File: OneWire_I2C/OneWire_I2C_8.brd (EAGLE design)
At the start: 22.2 x 28.2 mm, 14 parts, among them Q1 TP0602N3

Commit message: Added Schematic and board for DS2482-800
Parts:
- removed C1: (no value), SparkFun-Capacitors:0603-CAP
- removed Q1: TP0602N3, transistor-fet:TO-92
- removed R3: (no value), SparkFun-Resistors:AXIAL-0.4
- removed W1: DS2482-100, PuffinOneWIre:SOIC8
- added J2, J4, J5, J6, J7, J8: (no value), SparkFun-Connectors:1X03
- added J9: (no value), SparkFun-Connectors:1X06
- added SJ5: (no value), jumper:SJ
- added U$3: (no value), SparkFun-Electromechanical:STAND-OFF
- J1: device SparkFun-Connectors:1X05 -> SparkFun-Connectors:1X03
- J3: device SparkFun-Connectors:SCREWTERMINAL-3.5MM-3 -> SparkFun-Connectors:1X03
- R1, R2: device SparkFun-Resistors:0603-RES -> SparkFun-Passives:0603-RES
- SJ3: device jumper:SJ -> jumper:SJ_2
- U$1: value (none) -> DS2482-800; device SparkFun-Electromechanical:STAND-OFF-TIGHT -> Puffin:SOIC16
- U$2: device SparkFun-Electromechanical:STAND-OFF-TIGHT -> SparkFun-Electromechanical:STAND-OFF
- moved U$2 30.4 mm to (1.91, 2.54)
- moved J1 25.5 mm to (3.81, 22.9), turned to 90 degrees
- moved U$1 14.2 mm to (16.5, 16.5), turned to 90 degrees
- moved SJ3 13.4 mm to (5.08, 14.0)
- moved J3 8.64 mm to (8.89, 22.9), turned to 90 degrees
- moved SJ1 5.46 mm to (5.08, 6.35), turned to 0 degrees
- moved SJ2 5.46 mm to (5.08, 10.2), turned to 0 degrees
- moved R1 3.70 mm to (18.4, 6.35), turned to 0 degrees
- moved SJ4 3.70 mm to (14.6, 6.35), turned to 180 degrees
- moved R2 3.70 mm to (18.4, 10.2), turned to 0 degrees
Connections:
- removed net 1WR: J1.4, J3.2, Q1.3, W1.2
- removed net N$10: Q1.1, R3.P$1
- removed net N$3: R2.2, SJ3.2
- removed net N$4: R1.2, SJ4.2
- removed net PCTL: Q1.2, W1.6
- new net AD2: SJ3.2, U$1.6
- new net IO0: J1.2, J9.3, U$1.14
- new net IO1: J2.2, J9.2, U$1.15
- new net IO2: J3.2, U$1.16
- new net IO3: J4.2, U$1.1
- new net IO4: J5.2, U$1.12
- new net IO5: J6.2, U$1.11
- new net IO6: J7.2, U$1.10
- new net IO7: J8.2, U$1.9
- new net N$1: R1.1, SJ4.1
- new net N$2: R2.1, SJ5.1
- net AD0: now also U$1.8; no longer W1.8
- net AD1: now also U$1.7; no longer W1.7
- net GND: now also J1.3, J2.3, J4.3, J5.3, J6.3, J7.3, J8.3, J9.1, SJ3.3, U$1.13; no longer C1.2, J1.5, W1.3
- net SCL: now also J9.4, SJ4.2, U$1.2; no longer J1.2, SJ3.1, W1.4
- net SDA: now also J9.5, SJ5.2, U$1.3; no longer J1.3, SJ4.1, W1.5
- net VCC: now also J2.1, J4.1, J5.1, J6.1, J7.1, J8.1, J9.6, R1.2, R2.2, SJ3.1, U$1.4; no longer C1.1, R1.1, R2.1, R3.P$2, W1.1
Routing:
- net 1WR: track 42.4 -> 0.00 mm
- net IO0: track 0.00 -> 32.2 mm, vias 0 -> 2
- net IO1: track 0.00 -> 31.5 mm, vias 0 -> 2
- net AD2: track 0.00 -> 17.2 mm, vias 0 -> 2
- net AD0: track 9.08 -> 23.3 mm, vias 0 -> 2
- net IO3: track 0.00 -> 12.1 mm
- net SCL: track 23.7 -> 13.5 mm, vias 2 -> 0
- net IO7: track 0.00 -> 8.11 mm
- net IO4: track 0.00 -> 8.11 mm
- net N$10: track 7.93 -> 0.00 mm
- net IO2: track 0.00 -> 7.74 mm
- net IO6: track 0.00 -> 7.22 mm
- net IO5: track 0.00 -> 7.22 mm
- net PCTL: track 6.69 -> 0.00 mm
- net VCC: track 63.5 -> 69.3 mm
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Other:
- board size 22.2 x 28.2 mm -> 26.7 x 30.8 mm
- board text removed: "1WR"
- board text removed: "GND"
- board text removed: "SCL"
- board text removed: "SDA"
- board text removed: "VCC"

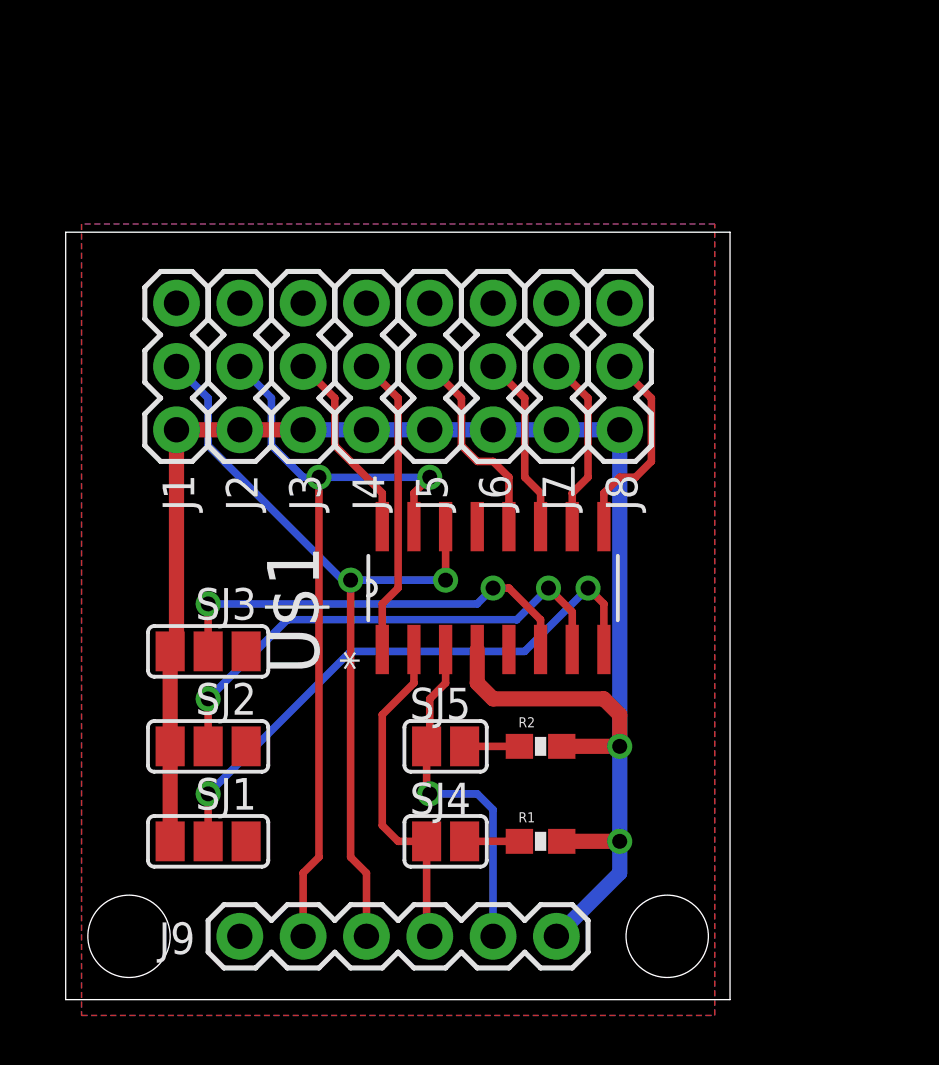
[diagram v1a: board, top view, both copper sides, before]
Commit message: Tweaks to I2C 1Wire bridge boards
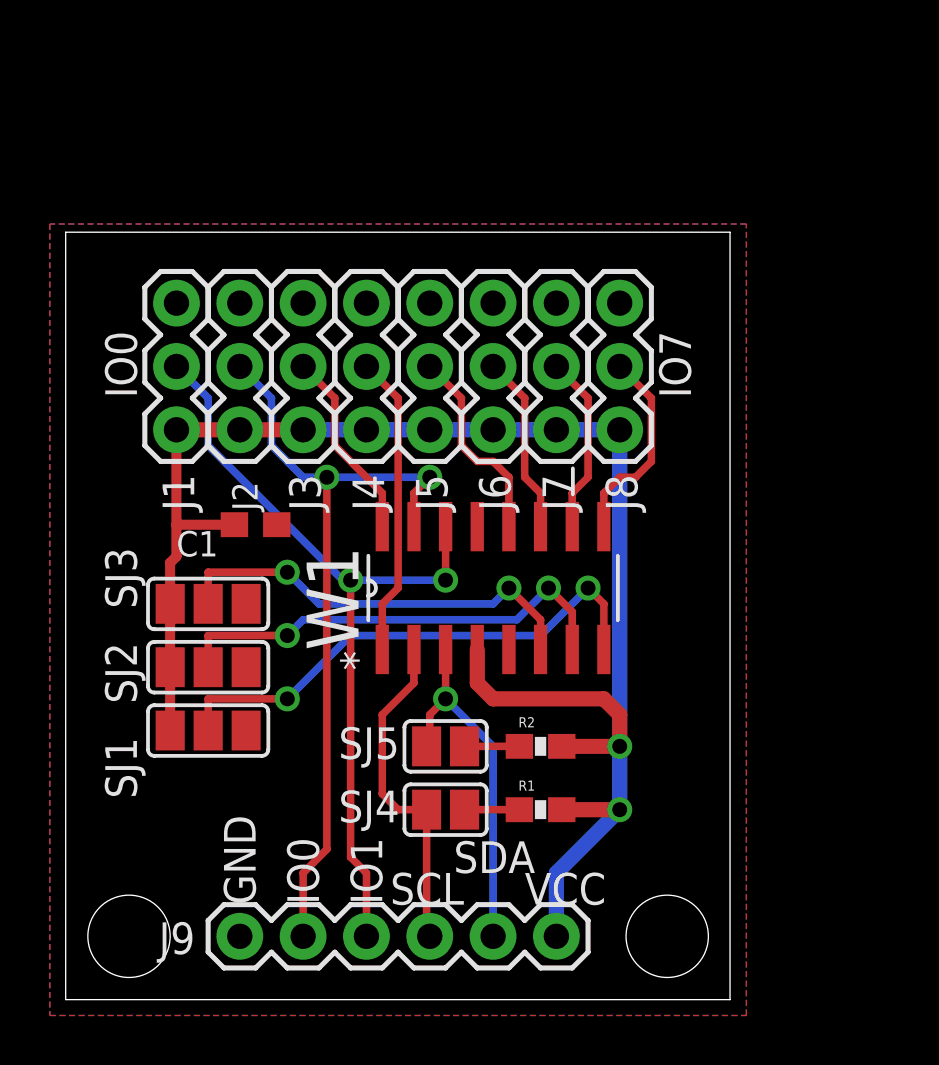
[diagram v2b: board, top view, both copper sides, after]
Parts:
- added C1: (no value), resistor:C0603
- moved SJ1 4.45 mm to (5.08, 10.8)
- moved SJ2 3.18 mm to (5.08, 13.3)
- moved SJ3 1.90 mm to (5.08, 15.9)
- moved R1 1.27 mm to (18.4, 7.62)
- moved SJ4 1.27 mm to (14.6, 7.62)
- renumbered U$1 to W1
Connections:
- net GND: now also C1.2
- net VCC: now also C1.1
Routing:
- net AD0: track 23.3 -> 21.1 mm
- net VCC: track 69.3 -> 67.2 mm
- net AD1: track 20.3 -> 18.6 mm
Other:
- board text added: "GND"
- board text added: "IO0"
- board text added: "IO1"
- board text added: "IO7"
- board text added: "SCL"
- board text added: "SDA"
- board text added: "VCC"

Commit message: Changed I2C pullup jumpers to single 3-way jumper
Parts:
- removed SJ5: (no value), jumper:SJ
- SJ4: device jumper:SJ -> jumper:SJ_2
- moved SJ4 4.02 mm to (18.4, 8.89), turned to 90 degrees
- moved R1 3.49 mm to (14.9, 7.62)
- moved R2 3.49 mm to (14.9, 10.2)
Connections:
- net N$1: now also R1.2; no longer R1.1
- net N$2: now also R2.2, SJ4.3; no longer R2.1, SJ5.1
- net SCL: now also R1.1; no longer SJ4.2
- net SDA: now also R2.1; no longer SJ5.2
- net VCC: now also SJ4.2; no longer R1.2, R2.2
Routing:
- net N$1: track 2.20 -> 2.75 mm
- net N$2: track 2.20 -> 2.75 mm
- net VCC: track 67.2 -> 67.1 mm, vias 2 -> 1
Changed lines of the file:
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@@
 <attribute name="VALUE" x="5.08" y="-0.635" size="1.27" layer="27"/>
 </element>
-<element name="R1" library="SparkFun-Passives" package="0603-RES" value="" x="18.415" y="7.62"/>
-<element name="R2" library="SparkFun-Passives" package="0603-RES" value="" x="18.415" y="10.16"/>
+<element name="R1" library="SparkFun-Passives" package="0603-RES" value="" x="14.9225" y="7.62"/>
+<element name="R2" library="SparkFun-Passives" package="0603-RES" value="" x="14.9225" y="10.16"/>
 <element name="SJ1" library="jumper" package="SJ_2" value="" x="5.08" y="10.795" smashed="yes">
 <attribute name="NAME" x="2.2225" y="8.0645" size="1.27" layer="25" ratio="10" rot="R90"/>
@@
 <attribute name="NAME" x="2.2225" y="15.6845" size="1.27" layer="25" ratio="10" rot="R90"/>
 <attribute name="VALUE" x="4.9799" y="15.875" size="0.02" layer="27"/>
-</element>
-<element name="SJ4" library="jumper" package="SJ" value="" x="14.605" y="7.62" smashed="yes" rot="R180">
-<attribute name="NAME" x="12.7635" y="8.382" size="1.27" layer="25" ratio="10" rot="R180"/>
-<attribute name="VALUE" x="14.2049" y="7.62" size="0.02" layer="27" rot="R180"/>
-</element>
-<element name="SJ5" library="jumper" package="SJ" value="" x="14.605" y="10.16" smashed="yes" rot="R180">
-<attribute name="NAME" x="12.7635" y="10.922" size="1.27" layer="25" ratio="10" rot="R180"/>
-<attribute name="VALUE" x="14.2049" y="10.16" size="0.02" layer="27" rot="R180"/>
 </element>
 <element name="W1" library="Puffin" package="SOIC16" value="DS2482-800" x="16.51" y="16.51" smashed="yes" rot="R90">
@@
 <attribute name="NAME" x="3.81" y="17.78" size="1.016" layer="25" font="vector" ratio="15"/>
 <attribute name="VALUE" x="6.35" y="17.145" size="1.27" layer="27"/>
+</element>
+<element name="SJ4" library="jumper" package="SJ_2" value="" x="18.415" y="8.89" smashed="yes" rot="R90">
+<attribute name="NAME" x="20.955" y="7.747" size="1.27" layer="25" ratio="10" rot="R90"/>
+<attribute name="VALUE" x="18.415" y="8.7899" size="0.02" layer="27" rot="R90"/>
 </element>
 </elements>
@@
 <contactref element="W1" pad="4"/>
 <contactref element="J9" pad="6"/>
-<contactref element="R2" pad="2"/>
-<contactref element="R1" pad="2"/>
 <contactref element="J1" pad="1"/>
 <contactref element="J8" pad="1"/>
@@
 <contactref element="SJ1" pad="1"/>
 <contactref element="SJ2" pad="1"/>
-<wire x1="21.59" y1="7.62" x2="21.59" y2="10.16" width="0.6096" layer="16"/>
 <wire x1="21.59" y1="22.86" x2="19.05" y2="22.86" width="0.6096" layer="16"/>
 <wire x1="19.05" y1="22.86" x2="16.51" y2="22.86" width="0.6096" layer="16"/>
@@
 <wire x1="13.97" y1="22.86" x2="11.43" y2="22.86" width="0.6096" layer="16"/>
 <wire x1="8.89" y1="22.86" x2="11.43" y2="22.86" width="0.6096" layer="16"/>
-<via x="21.59" y="10.16" extent="1-16" drill="0.6"/>
 <via x="21.59" y="7.62" extent="1-16" drill="0.6"/>
 <wire x1="3.81" y1="22.86" x2="6.35" y2="22.86" width="0.6096" layer="1"/>
 <wire x1="6.35" y1="22.86" x2="8.89" y2="22.86" width="0.6096" layer="1"/>
-<wire x1="15.875" y1="14.0462" x2="15.875" y2="12.7" width="0.6096" layer="1"/>
-<wire x1="15.875" y1="12.7" x2="16.51" y2="12.065" width="0.6096" layer="1"/>
-<wire x1="16.51" y1="12.065" x2="20.955" y2="12.065" width="0.6096" layer="1"/>
-<wire x1="20.955" y1="12.065" x2="21.59" y2="11.43" width="0.6096" layer="1"/>
-<wire x1="21.59" y1="11.43" x2="21.59" y2="10.16" width="0.6096" layer="1"/>
-<wire x1="21.59" y1="10.16" x2="21.59" y2="22.86" width="0.6096" layer="16"/>
-<wire x1="19.265" y1="10.16" x2="21.59" y2="10.16" width="0.6096" layer="1"/>
-<wire x1="19.265" y1="7.62" x2="21.59" y2="7.62" width="0.6096" layer="1"/>
+<wire x1="21.59" y1="7.62" x2="21.59" y2="22.86" width="0.6096" layer="16"/>
 <wire x1="21.59" y1="7.62" x2="19.05" y2="5.08" width="0.6096" layer="16"/>
 <wire x1="19.05" y1="5.08" x2="19.05" y2="2.54" width="0.6096" layer="16"/>
@@
 <contactref element="C1" pad="1"/>
 <wire x1="6.135" y1="19.05" x2="3.81" y2="19.05" width="0.4064" layer="1"/>
+<contactref element="SJ4" pad="2"/>
+<wire x1="21.59" y1="7.62" x2="21.59" y2="8.89" width="0.6096" layer="1"/>
+<wire x1="21.59" y1="8.89" x2="21.59" y2="10.795" width="0.6096" layer="1"/>
+<wire x1="21.59" y1="10.795" x2="20.32" y2="12.065" width="0.6096" layer="1"/>
+<wire x1="20.32" y1="12.065" x2="16.51" y2="12.065" width="0.6096" layer="1"/>
+<wire x1="16.51" y1="12.065" x2="15.875" y2="12.7" width="0.6096" layer="1"/>
+<wire x1="15.875" y1="12.7" x2="15.875" y2="13.335" width="0.6096" layer="1"/>
+<wire x1="18.415" y1="8.89" x2="21.59" y2="8.89" width="0.4064" layer="1"/>
+<wire x1="15.875" y1="13.335" x2="15.875" y2="14.0462" width="0" layer="19" extent="1-1"/>
 </signal>
 <signal name="AD0">
@@
 <contactref element="J9" pad="5"/>
 <contactref element="W1" pad="3"/>
-<contactref element="SJ5" pad="2"/>
+<contactref element="R2" pad="1"/>
+<wire x1="14.605" y1="14.0462" x2="14.605" y2="12.065" width="0.3048" layer="1"/>
+<wire x1="14.605" y1="12.065" x2="13.97" y2="11.43" width="0.3048" layer="1"/>
+<wire x1="13.97" y1="11.43" x2="13.97" y2="10.2625" width="0.3048" layer="1"/>
+<wire x1="13.97" y1="10.2625" x2="14.0725" y2="10.16" width="0.3048" layer="1"/>
 <via x="14.605" y="12.065" extent="1-16" drill="0.6"/>
-<wire x1="13.843" y1="10.16" x2="13.97" y2="10.287" width="0.3048" layer="1"/>
 <wire x1="16.51" y1="2.54" x2="16.51" y2="10.16" width="0.3048" layer="16"/>
 <wire x1="16.51" y1="10.16" x2="14.605" y2="12.065" width="0.3048" layer="16"/>
-<wire x1="14.605" y1="14.0462" x2="14.605" y2="12.065" width="0.3048" layer="1"/>
-<wire x1="13.97" y1="10.287" x2="13.97" y2="11.43" width="0.3048" layer="1"/>
-<wire x1="13.97" y1="11.43" x2="14.605" y2="12.065" width="0.3048" layer="1"/>
 </signal>
 <signal name="SCL">
 <contactref element="J9" pad="4"/>
 <contactref element="W1" pad="2"/>
-<contactref element="SJ4" pad="2"/>
-<wire x1="13.97" y1="2.54" x2="13.843" y2="2.667" width="0.3048" layer="1"/>
-<wire x1="13.843" y1="2.667" x2="13.843" y2="7.62" width="0.3048" layer="1"/>
-<wire x1="13.335" y1="14.0462" x2="13.335" y2="12.7" width="0.3048" layer="1"/>
-<wire x1="13.335" y1="12.7" x2="12.065" y2="11.43" width="0.3048" layer="1"/>
-<wire x1="12.065" y1="11.43" x2="12.065" y2="8.255" width="0.3048" layer="1"/>
-<wire x1="12.065" y1="8.255" x2="12.7" y2="7.62" width="0.3048" layer="1"/>
-<wire x1="12.7" y1="7.62" x2="13.843" y2="7.62" width="0.3048" layer="1"/>
+<wire x1="13.97" y1="2.54" x2="13.97" y2="5.08" width="0.3048" layer="1"/>
+<wire x1="13.97" y1="5.08" x2="12.7" y2="6.35" width="0.3048" layer="1"/>
+<wire x1="12.7" y1="6.35" x2="12.7" y2="7.62" width="0.3048" layer="1"/>
+<wire x1="12.7" y1="7.62" x2="12.7" y2="11.43" width="0.3048" layer="1"/>
+<wire x1="12.7" y1="11.43" x2="13.335" y2="12.065" width="0.3048" layer="1"/>
+<wire x1="13.335" y1="12.065" x2="13.335" y2="14.0462" width="0.3048" layer="1"/>
+<contactref element="R1" pad="1"/>
+<wire x1="14.0725" y1="7.62" x2="12.7" y2="7.62" width="0.3048" layer="1"/>
 </signal>
 <signal name="N$1">
-<contactref element="R1" pad="1"/>
 <contactref element="SJ4" pad="1"/>
-<wire x1="15.367" y1="7.62" x2="17.565" y2="7.62" width="0.3048" layer="1"/>
+<contactref element="R1" pad="2"/>
+<wire x1="18.415" y1="7.366" x2="17.399" y2="7.366" width="0.4064" layer="1"/>
+<wire x1="17.399" y1="7.366" x2="17.145" y2="7.62" width="0.4064" layer="1"/>
+<wire x1="15.7725" y1="7.62" x2="17.145" y2="7.62" width="0.4064" layer="1"/>
 </signal>
 <signal name="N$2">
-<contactref element="R2" pad="1"/>
-<contactref element="SJ5" pad="1"/>
-<wire x1="15.367" y1="10.16" x2="17.565" y2="10.16" width="0.3048" layer="1"/>
+<contactref element="SJ4" pad="3"/>
+<contactref element="R2" pad="2"/>
+<wire x1="18.415" y1="10.414" x2="17.399" y2="10.414" width="0.4064" layer="1"/>
+<wire x1="15.7725" y1="10.16" x2="17.145" y2="10.16" width="0.4064" layer="1"/>
+<wire x1="17.145" y1="10.16" x2="17.399" y2="10.414" width="0.4064" layer="1"/>
 </signal>
 </signals>

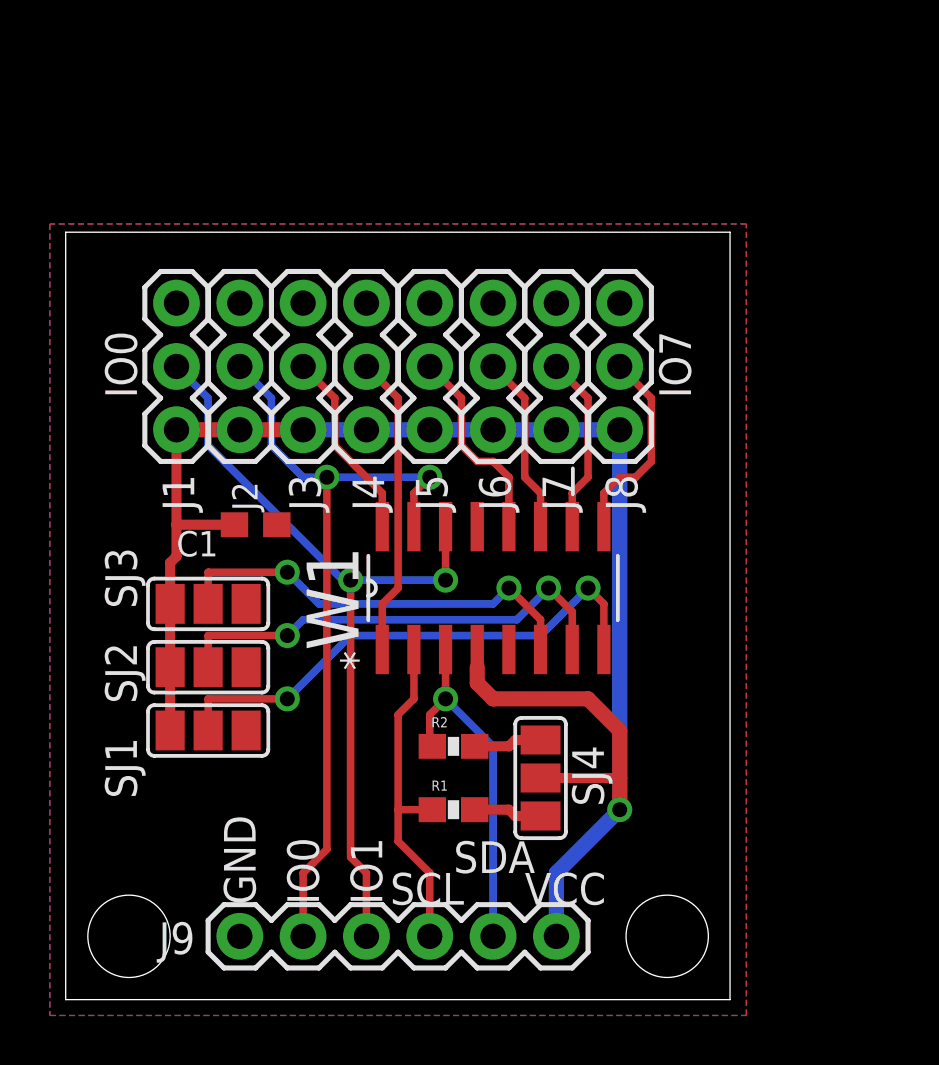
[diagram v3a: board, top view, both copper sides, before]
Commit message: Added 8 port OneWire I2C bridge with Extender
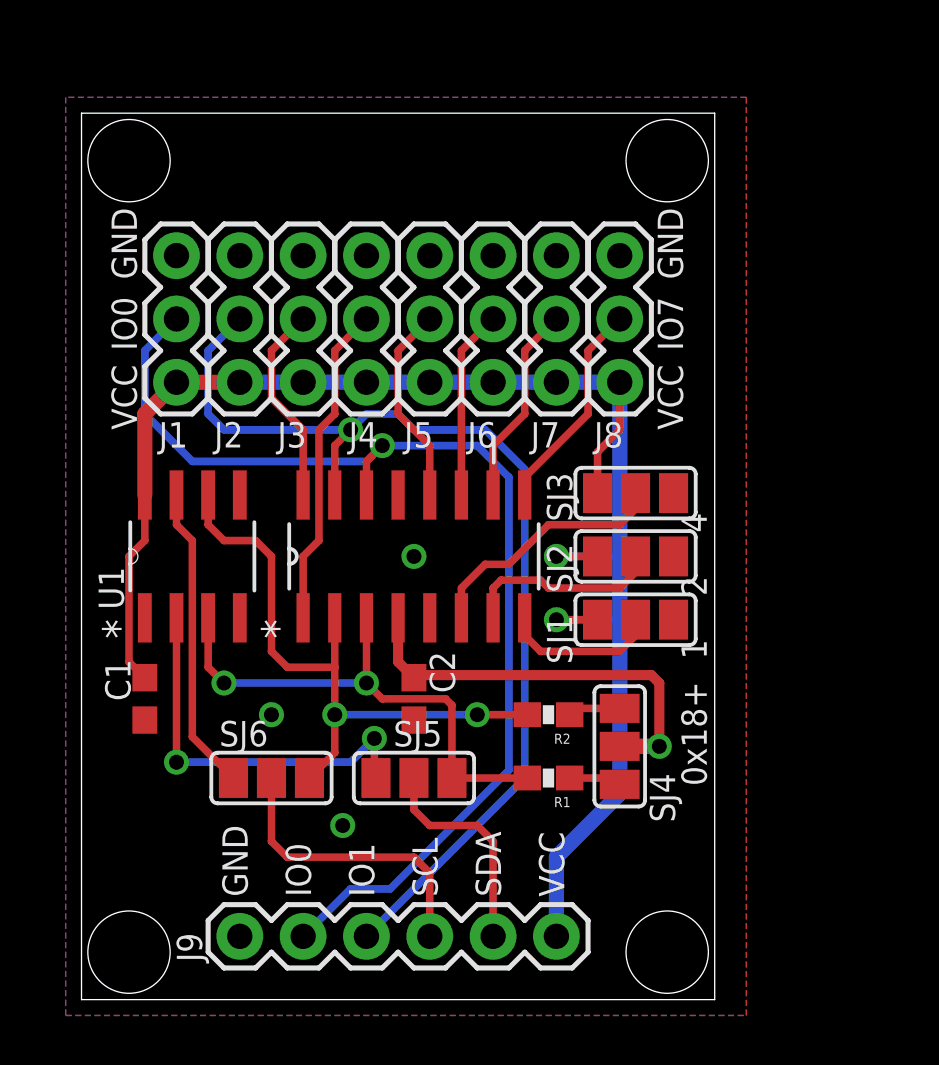
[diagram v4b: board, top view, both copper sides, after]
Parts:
- added C2: (no value), resistor:C0603
- added SJ5, SJ6: (no value), jumper:SJ_2
- added U$1, U$4: (no value), SparkFun-Electromechanical:STAND-OFF
- added U1: P82B715D, Texas Instruments_By_element14_Batch_1:SOIC127P600X175-8N
- moved SJ1 17.7 mm to (22.2, 15.2)
- moved SJ2 17.7 mm to (22.2, 17.8)
- moved SJ3 17.7 mm to (22.2, 20.3)
- moved C1 8.28 mm to (2.54, 12.1), turned to 270 degrees
- moved R1 4.02 mm to (18.7, 8.89), turned to 180 degrees
- moved R2 4.02 mm to (18.7, 11.4), turned to 180 degrees
- moved SJ4 3.42 mm to (21.6, 10.2)
- moved W1 3.42 mm to (13.3, 17.8)
- moved J1 1.91 mm to (3.81, 24.8)
- moved J2 1.91 mm to (6.35, 24.8)
- moved J3 1.91 mm to (8.89, 24.8)
- moved J4 1.91 mm to (11.4, 24.8)
- moved J5 1.91 mm to (14.0, 24.8)
- moved J6 1.91 mm to (16.5, 24.8)
- moved J7 1.91 mm to (19.1, 24.8)
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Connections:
- new net LSCL: J9.4, SJ6.2
- new net LSDA: J9.5, SJ5.2
- new net LX: SJ5.1, U1.2
- new net LY: SJ6.1, U1.7
- net GND: now also C2.2, U1.4
- net IO0: now also J9.2; no longer J9.3
- net IO1: now also J9.3; no longer J9.2
- net N$1: now also R2.1, SJ4.3; no longer R1.2, SJ4.1
- net N$2: now also R1.1, SJ4.1; no longer R2.2, SJ4.3
- net SCL: now also R2.2, SJ6.3, U1.6; no longer J9.4, R1.1
- net SDA: now also R1.2, SJ5.3, U1.3; no longer J9.5, R2.1
- net VCC: now also C2.1, U1.8
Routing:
- net VCC: track 67.1 -> 85.6 mm, vias 1 -> 3
- net LX: track 0.00 -> 16.0 mm, vias 0 -> 2
- net AD0: track 21.1 -> 6.32 mm, vias 2 -> 0
- net IO0: track 32.2 -> 45.5 mm, vias 2 -> 1
- net LY: track 0.00 -> 12.3 mm
- net LSCL: track 0.00 -> 12.0 mm
- net SCL: track 13.7 -> 25.4 mm, vias 0 -> 2
- net IO1: track 31.6 -> 42.7 mm, vias 2 -> 1
- net AD1: track 18.6 -> 8.07 mm, vias 2 -> 0
- net LSDA: track 0.00 -> 8.78 mm
- net AD2: track 17.1 -> 10.1 mm, vias 2 -> 0
- net SDA: track 14.5 -> 21.0 mm, vias 1 -> 2
- net IO3: track 12.1 -> 13.0 mm
- net IO6: track 7.22 -> 8.11 mm
- net N$1: track 2.75 -> 2.11 mm
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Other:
- board size 26.7 x 30.8 mm -> 25.4 x 35.6 mm
- board text added: "0x18+"
- board text added: "1"
- board text added: "2"
- board text added: "4"
